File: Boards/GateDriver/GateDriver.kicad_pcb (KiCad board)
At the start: 4 copper layers, 112.5 x 120 mm, 115 parts, among them J1 1548129, J3 1548129, J4 5-106505-2, J5 1987724, J6 1987724, J7 1987724, U2 PUCC5880QDFCQ1

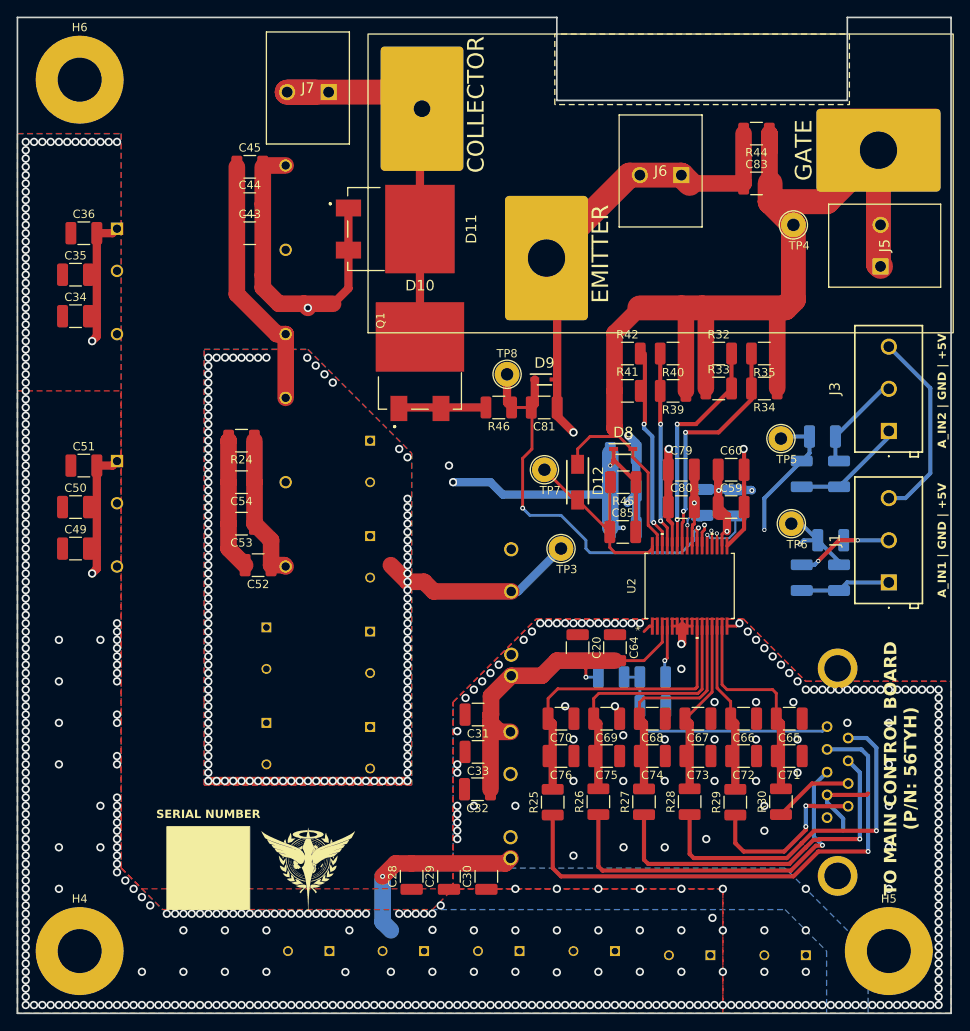
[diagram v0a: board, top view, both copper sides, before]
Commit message: Update Gate Driver to use non NDA BS Chip
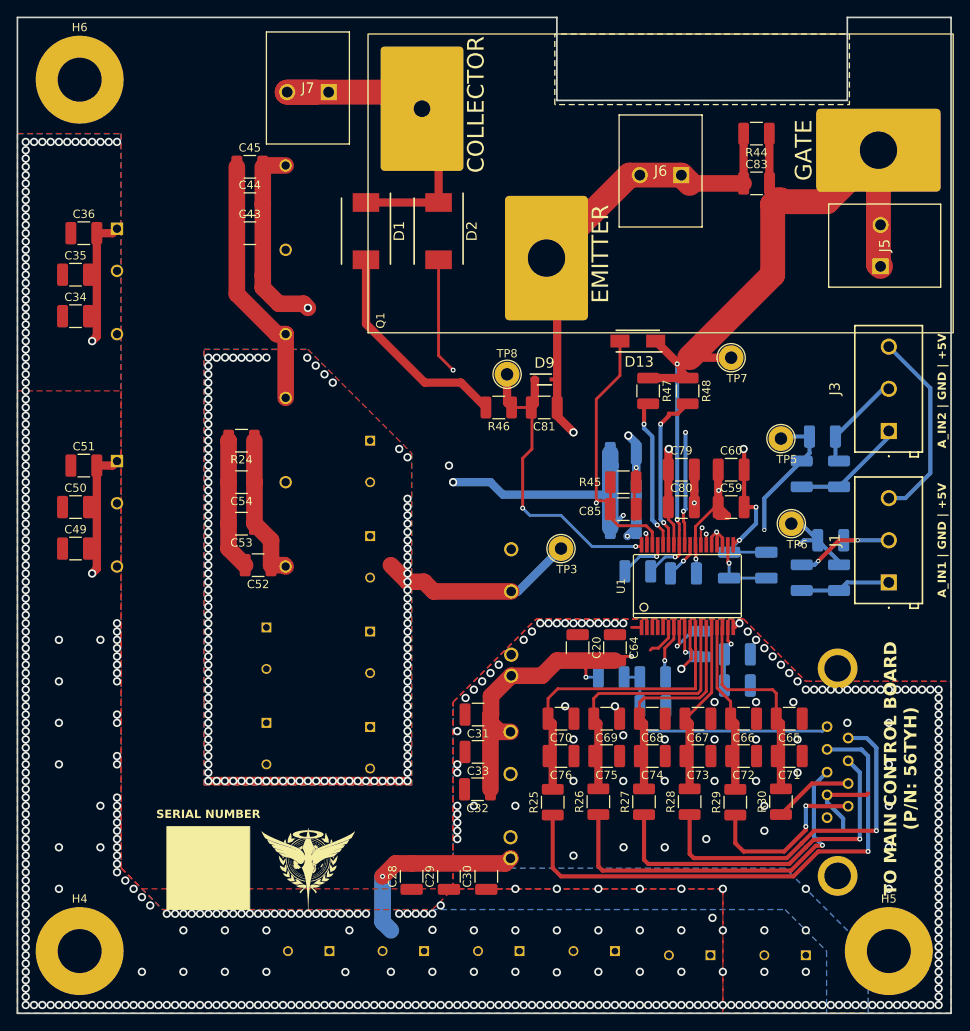
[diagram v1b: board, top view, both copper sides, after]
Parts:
- removed C58: 1uF, Capacitor_SMD:C_1210_3225Metric_Pad1.33x2.70mm_HandSolder
- removed D10, D11: VS-30CDU06HM3_I, InverterCom:VS30CDU06HM3I
- removed D12: MBRA340T3G, InverterCom:DIOM5226X220N
- removed D8: BAT54WS-7-F, InverterCom:SOD2513X120N
- removed R33, R34, R35: 4.7, Resistor_SMD:R_1210_3225Metric_Pad1.30x2.65mm_HandSolder
- removed R39, R40, R41, R42: 8.2, Resistor_SMD:R_1210_3225Metric_Pad1.30x2.65mm_HandSolder
- removed REF**: ESD-Logo_13.2x12mm_SilkScreen, Symbol:ESD-Logo_13.2x12mm_SilkScreen
- removed REF**: KiCad-Logo2_8mm_SilkScreen, Symbol:KiCad-Logo2_8mm_SilkScreen
- removed REF**: OSHW-Logo2_14.6x12mm_SilkScreen, Symbol:OSHW-Logo2_14.6x12mm_SilkScreen
- removed REF**: WEEE-Logo_8.4x12mm_SilkScreen, Symbol:WEEE-Logo_8.4x12mm_SilkScreen
- removed TP4: TestPoint, TestPoint:TestPoint_Loop_D2.54mm_Drill1.5mm_Beaded
- removed U2: PUCC5880QDFCQ1, InverterCom:SSOP32_DFC_TEX-M
- added C22: 4.7uF, Capacitor_SMD:C_1210_3225Metric_Pad1.33x2.70mm_HandSolder, B.Cu at (161.8, 120.5)
- added C23: 4.7uF, Capacitor_SMD:C_1210_3225Metric_Pad1.33x2.70mm_HandSolder, B.Cu at (160.8, 106.0)
- added C63: 1uF, Capacitor_SMD:C_1210_3225Metric_Pad1.33x2.70mm_HandSolder, B.Cu at (155.2, 107.0)
- added C87: 100nF, Capacitor_SMD:C_1210_3225Metric_Pad1.33x2.70mm_HandSolder, B.Cu at (161.8, 116.8)
- added C88: 100nF, Capacitor_SMD:C_1210_3225Metric_Pad1.33x2.70mm_HandSolder, B.Cu at (165.2, 106.0)
- added D1: S3N, InverterCom:DIOM8059X265N, F.Cu at (117.0, 65.8)
- added D13: MBRA340T3G, InverterCom:DIOM5226X220N, F.Cu at (149.8, 79.0)
- added D2: S3N, InverterCom:DIOM8059X265N, F.Cu at (125.8, 65.8)
- added R47: 1.5, Resistor_SMD:R_1210_3225Metric_Pad1.30x2.65mm_HandSolder, F.Cu at (151.0, 85.0)
- added R48: 1.5, Resistor_SMD:R_1210_3225Metric_Pad1.30x2.65mm_HandSolder, F.Cu at (155.8, 85.0)
- added U1: UCC5870QDWJRQ1, InverterCom:DWJ0036A, F.Cu at (155.7, 108.5)
- C85: value 10nF -> 2.2nF
- R32: value 4.7 -> 47k; moved to B.Cu
- R44: value 10k -> 1k
- R45: value 33 -> 100
- moved R32 35.1 mm to (157.2, 115.5), turned to -90 degrees
- moved TP7 26.2 mm to (161.0, 81.0)
- moved C61 11.4 mm to (149.8, 106.8), turned to 180 degrees
- moved C85 2.75 mm to (148.0, 99.2)
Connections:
- net DESAT renamed Net-(D9-K)
- C61 pad 1: IGBT_EMITTER -> IGBT_GATE
- C85 pad 1: Net-(D12-A) -> Net-(D13-A)
- C85 pad 2: ISO_GATE_DRIVE_+15V -> IGBT_EMITTER
- R32 pad 1: IGBT_GATE -> Net-(U1-nFLT2_DOUT)
- R32 pad 2: Net-(U2-OUTH2) -> +5V
- R45 pad 1: ISO_GATE_DRIVE_+15V -> IGBT_EMITTER
- R45 pad 2: Net-(D12-A) -> Net-(D13-A)
- TP7 pad 1: Net-(D12-A) -> IGBT_GATE
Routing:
- net Net-(D13-A): track 0.00 -> 74.6 mm, vias 0 -> 2
- net IGBT_GATE: track 140.4 -> 103.0 mm, vias 0 -> 3
- net ISO_GATE_DRIVE_+15V: track 139.5 -> 103.1 mm
- net Net-(U2-OUTH1): track 29.0 -> 0.00 mm, vias 2 -> 0
- net Net-(U2-OUTH2): track 27.2 -> 0.00 mm, vias 2 -> 0
- net Net-(D12-A): track 24.8 -> 0.00 mm
- net Net-(U2-OUTL2): track 24.1 -> 0.00 mm, vias 2 -> 0
- net Net-(U2-OUTL1): track 23.5 -> 0.00 mm, vias 2 -> 0
- net Net-(U1-OUTL): track 0.00 -> 19.4 mm, vias 0 -> 2
- net Net-(U1-OUTH): track 0.00 -> 18.2 mm, vias 0 -> 2
- net Net-(D1-A): track 10.5 -> 26.3 mm
- net IGBT_EMITTER: track 216.2 -> 231.6 mm, vias 132 -> 134
- net Net-(D9-K): track 51.1 -> 39.1 mm
- net Net-(U1-VREG2): track 0.00 -> 8.57 mm, vias 0 -> 1
- net ISO_GATE_DRIVE_-9V: track 85.5 -> 93.7 mm, vias 3 -> 5
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- added copper zone on In1.Cu, net IGBT_EMITTER

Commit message: Update Layouts
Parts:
- R23, R32: value 47k -> 10k
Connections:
- U1 pad 2: unconnected-(U1-NC-Pad2) -> GND
- U1 pad 3: unconnected-(U1-NC-Pad3) -> GND
- U1 pad 4: unconnected-(U1-NC-Pad4) -> GND
- U1 pad 5: unconnected-(U1-NC-Pad5) -> GND
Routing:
- net GND: track 21.9 -> 25.2 mm
- net IGBT_EMITTER: vias 134 -> 165

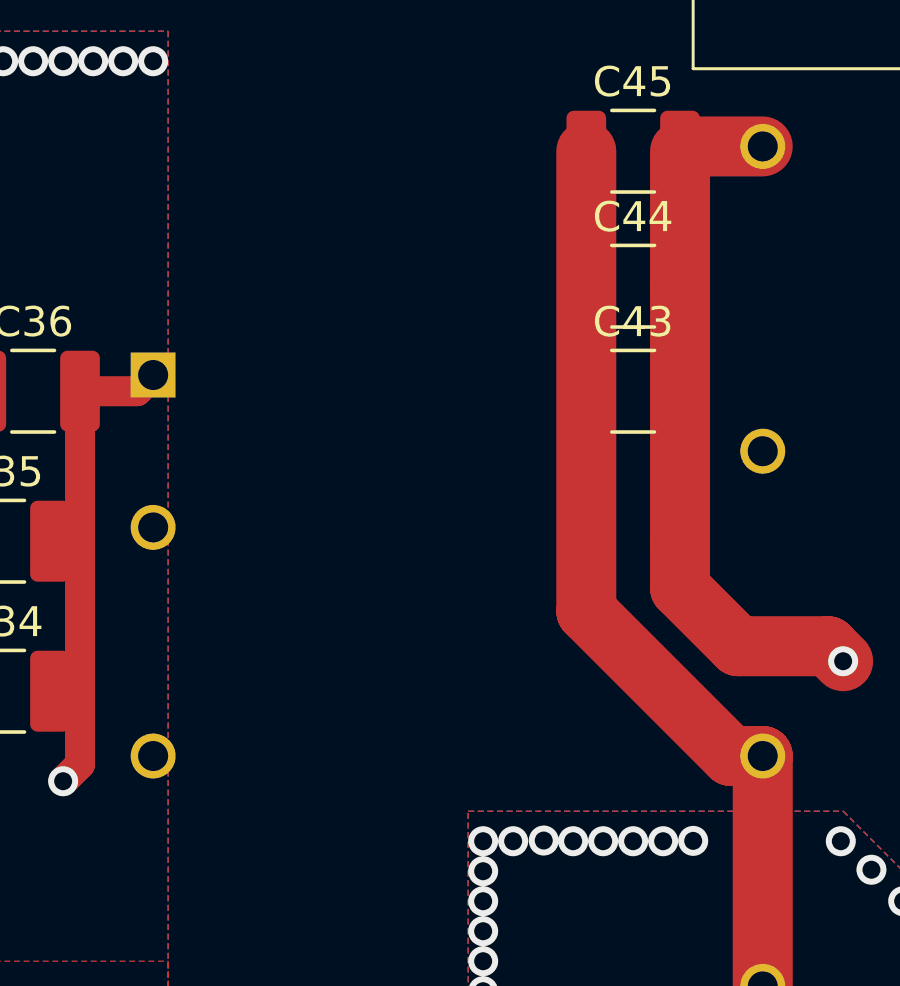
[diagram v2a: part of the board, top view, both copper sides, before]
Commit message: Update board soldermask
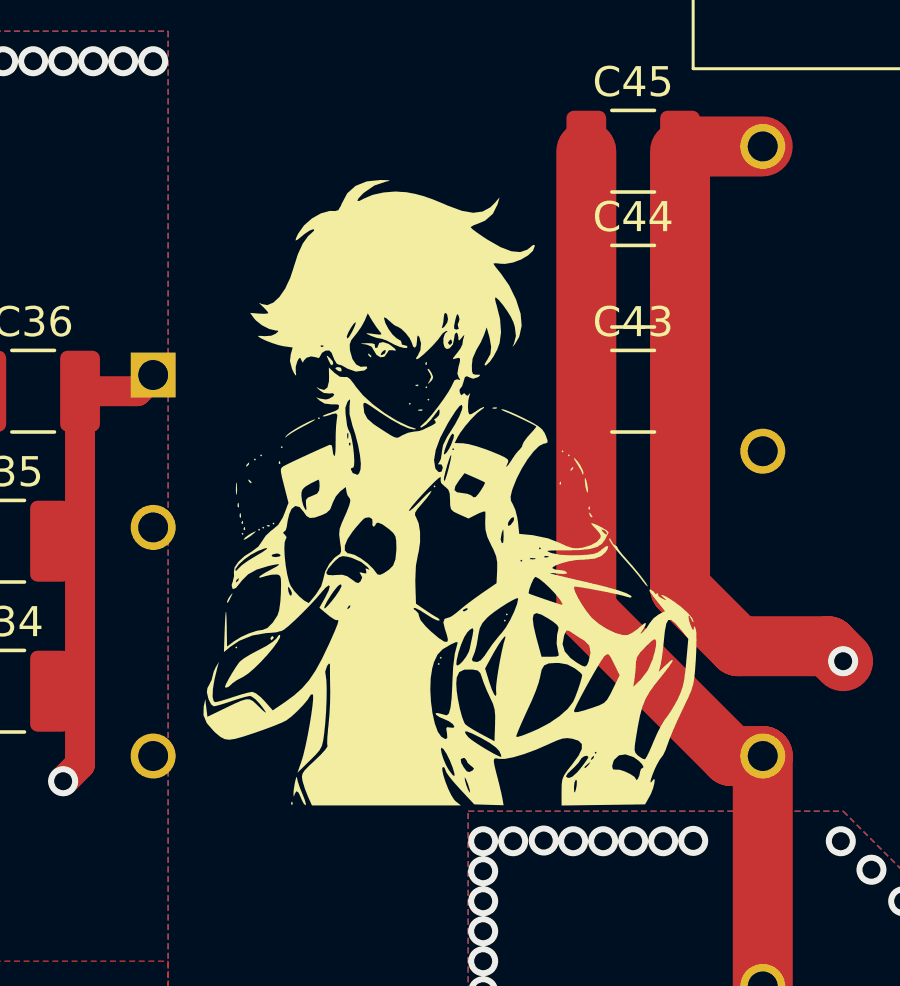
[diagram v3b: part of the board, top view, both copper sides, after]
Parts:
- added G***: LOGO, InverterCom:Char_SetsunaFSeiei_20mm, F.Cu at (97.0, 69.0)
